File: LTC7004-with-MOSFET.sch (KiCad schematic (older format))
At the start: 6 parts, among them J1 Conn_01x02, J2 Grove-I2C-connector, Q1 Q_NMOS_SGD, U1 GateDriver_LTC7004

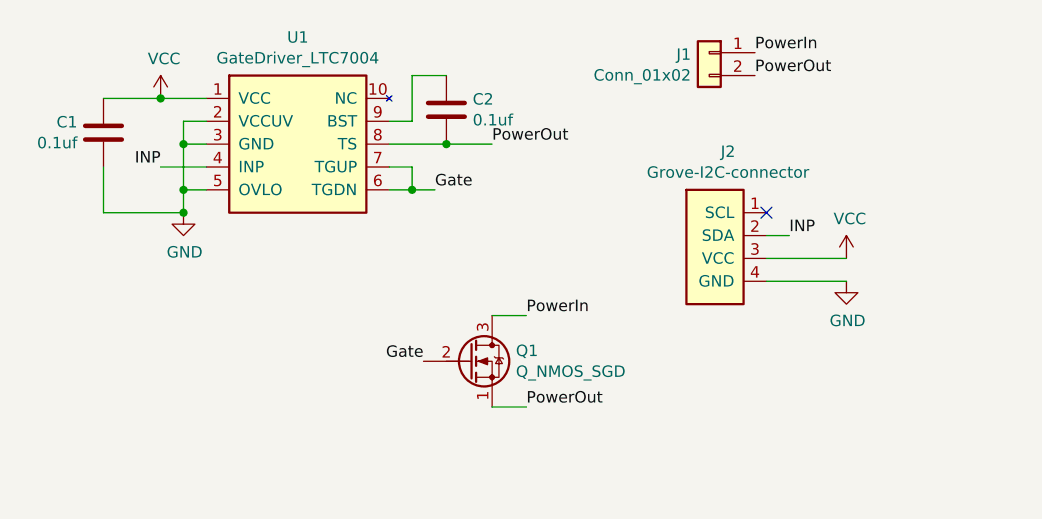
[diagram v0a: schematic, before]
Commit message: Add second mosfet
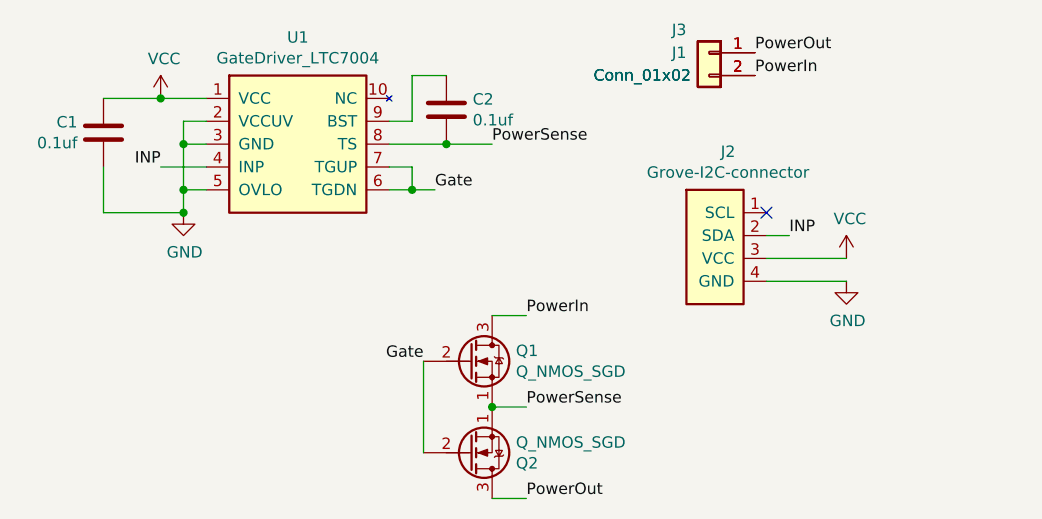
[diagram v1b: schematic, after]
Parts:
- added J3: Conn_01x02, TerminalBlock_Phoenix:TerminalBlock_Phoenix_MKDS-1,5-2-5.08_1x02_P5.08mm_Horizontal, symbol Connector_Generic:Conn_01x02
- added Q2: Q_NMOS_SGD, my-kicad-footprints:DFN5, symbol Device:Q_NMOS_SGD
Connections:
- net Gate: now also Q2.2 (G)
- net PowerIn: now also J1.2 (Pin_2), J3.2 (Pin_2); no longer J1.1 (Pin_1)
- net PowerOut: now also J1.1 (Pin_1), J3.1 (Pin_1), Q2.3 (D); no longer C2.2, J1.2 (Pin_2), Q1.1 (S), U1.8 (TS)
- new net PowerSense: C2.2, Q1.1 (S), Q2.1 (S), U1.8 (TS)
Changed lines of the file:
@@
 U 1 1 60D2F53E
 P 7450 2550
-F 0 "J1" H 7530 2542 50  0000 L CNN
+F 0 "J1" H 7550 2550 50  0000 L CNN
 F 1 "Conn_01x02" H 7530 2451 50  0000 L CNN
 F 2 "my-kicad-footprints:Terminal_9.52mm_1x02_1714971" H 7450 2550 50  0001 C CNN
@@
 	-1   0    0    -1
 $EndComp
+Text Label 7650 2650 0    50   ~ 0
+PowerIn
 Text Label 7650 2550 0    50   ~ 0
-PowerIn
-Text Label 7650 2650 0    50   ~ 0
 PowerOut
 $Comp
@@
 	6150 3150 6250 3150
 Text Label 6500 2950 0    50   ~ 0
-PowerOut
+PowerSense
 Wire Wire Line
 	6500 2950 6300 2950
@@
 Text Label 6200 3900 2    50   ~ 0
 Gate
-Text Label 6650 4100 0    50   ~ 0
+Text Label 6650 4500 0    50   ~ 0
 PowerOut
 Wire Wire Line
@@
 Wire Wire Line
 	6650 3700 6500 3700
+$Comp
+L Connector_Generic:Conn_01x02 J3
+U 1 1 61133E0A
+P 7450 2550
+F 0 "J3" H 7550 2650 50  0000 L CNN
+F 1 "Conn_01x02" H 7530 2451 50  0000 L CNN
+F 2 "TerminalBlock_Phoenix:TerminalBlock_Phoenix_MKDS-1,5-2-5.08_1x02_P5.08mm_Horizontal" H 7450 2550 50  0001 C CNN
+F 3 "~" H 7450 2550 50  0001 C CNN
+	1    7450 2550
+	-1   0    0    -1
+$EndComp
+$Comp
+L Device:Q_NMOS_SGD Q2
+U 1 1 6135776B
+P 6400 4300
+F 0 "Q2" H 6604 4346 50  0000 L CNN
+F 1 "Q_NMOS_SGD" H 6604 4255 50  0000 L CNN
+F 2 "my-kicad-footprints:DFN5" H 6600 4400 50  0001 C CNN
+F 3 "~" H 6400 4300 50  0001 C CNN
+	1    6400 4300
+	1    0    0    1
+$EndComp
+Connection ~ 6500 4100
+Wire Wire Line
+	6200 3900 6200 4300
+Wire Wire Line
+	6650 4500 6500 4500
+Text Label 6650 4100 0    50   ~ 0
+PowerSense
 $EndSCHEMATC

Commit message: Add condensor, resistor and varistor
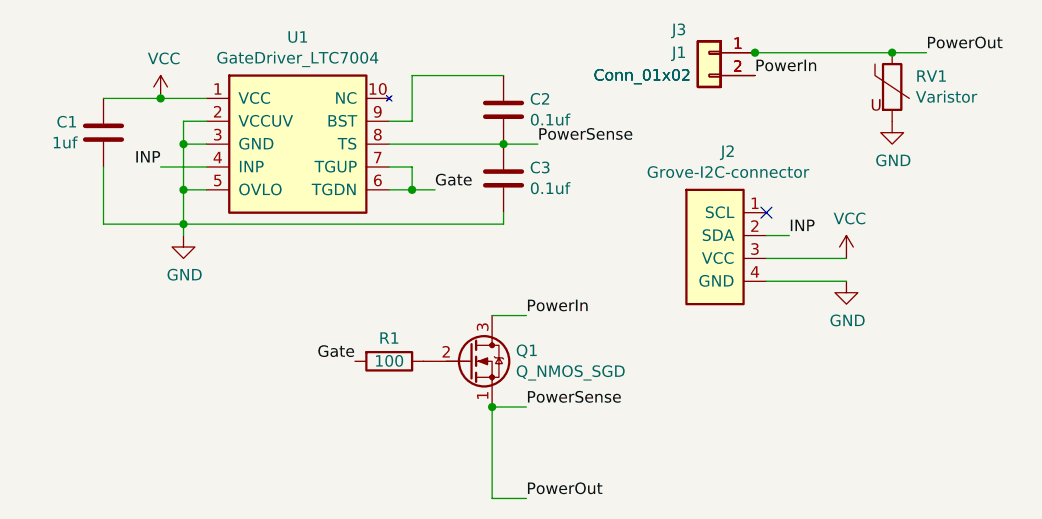
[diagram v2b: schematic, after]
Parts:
- removed Q2: Q_NMOS_SGD, my-kicad-footprints:DFN5, symbol Device:Q_NMOS_SGD
- added C3: 0.1uf, Capacitor_SMD:C_0603_1608Metric, symbol Device:C
- added R1: 100, Resistor_SMD:R_0603_1608Metric, symbol Device:R
- added RV1: Varistor, Resistor_SMD:R_1206_3216Metric, symbol Device:Varistor
- C1: value 0.1uf -> 1uf
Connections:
- net PowerSense is gone; now on net PowerOut: C2.2, Q1.1 (S), U1.8 (TS)
- net GND: now also C3.2, RV1.2
- net Gate: now also R1.2; no longer Q1.2 (G)
- net PowerOut: now also C3.1, RV1.1
- new net: Q1.2 (G), R1.1
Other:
- moved on the sheet: C2
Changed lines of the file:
@@
 L power:GND #PWR0101
 U 1 1 60D2D6A8
-P 5150 3250
-F 0 "#PWR0101" H 5150 3000 50  0001 C CNN
-F 1 "GND" H 5155 3077 50  0000 C CNN
-F 2 "" H 5150 3250 50  0001 C CNN
-F 3 "" H 5150 3250 50  0001 C CNN
-	1    5150 3250
+P 5150 3350
+F 0 "#PWR0101" H 5150 3100 50  0001 C CNN
+F 1 "GND" H 5155 3177 50  0000 C CNN
+F 2 "" H 5150 3350 50  0001 C CNN
+F 3 "" H 5150 3350 50  0001 C CNN
+	1    5150 3350
 	1    0    0    -1
 $EndComp
@@
 $EndComp
 Wire Wire Line
-	5150 3250 5150 3150
-Wire Wire Line
 	5150 2850 5250 2850
 Wire Wire Line
@@
 L Device:C C2
 U 1 1 60D2EC29
-P 6300 2800
-F 0 "C2" H 6415 2846 50  0000 L CNN
-F 1 "0.1uf" H 6415 2755 50  0000 L CNN
-F 2 "Capacitor_SMD:C_0603_1608Metric" H 6338 2650 50  0001 C CNN
-F 3 "~" H 6300 2800 50  0001 C CNN
-	1    6300 2800
-	1    0    0    -1
-$EndComp
-Wire Wire Line
-	6300 2950 6050 2950
+P 6550 2800
+F 0 "C2" H 6665 2846 50  0000 L CNN
+F 1 "0.1uf" H 6665 2755 50  0000 L CNN
+F 2 "Capacitor_SMD:C_0603_1608Metric" H 6588 2650 50  0001 C CNN
+F 3 "~" H 6550 2800 50  0001 C CNN
+	1    6550 2800
+	1    0    0    -1
+$EndComp
 Wire Wire Line
 	6150 2850 6150 2650
-Wire Wire Line
-	6150 2650 6300 2650
 Wire Wire Line
 	6050 2850 6150 2850
@@
 Text Label 7650 2650 0    50   ~ 0
 PowerIn
-Text Label 7650 2550 0    50   ~ 0
-PowerOut
 $Comp
 L my-kicad-symbols:Grove-I2C-connector J2
@@
 Wire Wire Line
 	6150 3150 6250 3150
-Text Label 6500 2950 0    50   ~ 0
+Text Label 6700 2950 0    50   ~ 0
 PowerSense
-Wire Wire Line
-	6500 2950 6300 2950
-Connection ~ 6300 2950
 $Comp
 L Device:C C1
@@
 P 4800 2900
 F 0 "C1" H 4686 2854 50  0000 R CNN
-F 1 "0.1uf" H 4686 2945 50  0000 R CNN
+F 1 "1uf" H 4686 2945 50  0000 R CNN
 F 2 "Capacitor_SMD:C_0603_1608Metric" H 4838 2750 50  0001 C CNN
 F 3 "~" H 4800 2900 50  0001 C CNN
@@
 	5050 2750 4800 2750
 Connection ~ 5050 2750
-Wire Wire Line
-	4800 3050 4800 3250
-Wire Wire Line
-	4800 3250 5150 3250
-Connection ~ 5150 3250
 $Comp
 L Device:Q_NMOS_SGD Q1
@@
 	1    0    0    -1
 $EndComp
-Text Label 6200 3900 2    50   ~ 0
+Text Label 5900 3900 2    50   ~ 0
 Gate
 Text Label 6650 4500 0    50   ~ 0
@@
 	-1   0    0    -1
 $EndComp
-$Comp
-L Device:Q_NMOS_SGD Q2
-U 1 1 6135776B
-P 6400 4300
-F 0 "Q2" H 6604 4346 50  0000 L CNN
-F 1 "Q_NMOS_SGD" H 6604 4255 50  0000 L CNN
-F 2 "my-kicad-footprints:DFN5" H 6600 4400 50  0001 C CNN
-F 3 "~" H 6400 4300 50  0001 C CNN
-	1    6400 4300
-	1    0    0    1
-$EndComp
-Connection ~ 6500 4100
-Wire Wire Line
-	6200 3900 6200 4300
 Wire Wire Line
 	6650 4500 6500 4500
 Text Label 6650 4100 0    50   ~ 0
 PowerSense
+Connection ~ 6550 2950
+Wire Wire Line
+	6550 2950 6700 2950
+Wire Wire Line
+	6050 2950 6550 2950
+Wire Wire Line
+	6150 2650 6550 2650
+Wire Wire Line
+	5150 3150 5150 3300
+Wire Wire Line
+	6550 3300 6550 3250
+Wire Wire Line
+	4800 3050 4800 3300
+Wire Wire Line
+	4800 3300 5150 3300
+Connection ~ 5150 3300
+Wire Wire Line
+	5150 3300 5150 3350
+Wire Wire Line
+	5150 3300 6550 3300
+Wire Wire Line
+	6500 4500 6500 4100
+Connection ~ 6500 4100
+$Comp
+L Device:R R1
+U 1 1 61728E19
+P 6050 3900
+F 0 "R1" V 5950 3900 50  0000 C CNN
+F 1 "100" V 6050 3900 50  0000 C CNN
+F 2 "Resistor_SMD:R_0603_1608Metric" V 5980 3900 50  0001 C CNN
+F 3 "~" H 6050 3900 50  0001 C CNN
+	1    6050 3900
+	0    1    1    0
+$EndComp
+$Comp
+L Device:Varistor RV1
+U 1 1 6172D250
+P 8250 2700
+F 0 "RV1" H 8353 2746 50  0000 L CNN
+F 1 "Varistor" H 8353 2655 50  0000 L CNN
+F 2 "Resistor_SMD:R_1206_3216Metric" V 8180 2700 50  0001 C CNN
+F 3 "~" H 8250 2700 50  0001 C CNN
+	1    8250 2700
+	1    0    0    -1
+$EndComp
+Text Label 8400 2550 0    50   ~ 0
+PowerOut
+$Comp
+L Device:C C3
+U 1 1 61723A07
+P 6550 3100
+F 0 "C3" H 6665 3146 50  0000 L CNN
+F 1 "0.1uf" H 6665 3055 50  0000 L CNN
+F 2 "Capacitor_SMD:C_0603_1608Metric" H 6588 2950 50  0001 C CNN
+F 3 "~" H 6550 3100 50  0001 C CNN
+	1    6550 3100
+	1    0    0    -1
+$EndComp
+Wire Wire Line
+	8400 2550 8250 2550
+Connection ~ 7650 2550
+Connection ~ 8250 2550
+Wire Wire Line
+	8250 2550 7650 2550
+$Comp
+L power:GND #PWR0105
+U 1 1 61732F6D
+P 8250 2850
+F 0 "#PWR0105" H 8250 2600 50  0001 C CNN
+F 1 "GND" H 8255 2677 50  0000 C CNN
+F 2 "" H 8250 2850 50  0001 C CNN
+F 3 "" H 8250 2850 50  0001 C CNN
+	1    8250 2850
+	1    0    0    -1
+$EndComp
 $EndSCHEMATC
